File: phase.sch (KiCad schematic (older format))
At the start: 30 parts, among them U4 INA240A1PW, U5 UCC21520DW

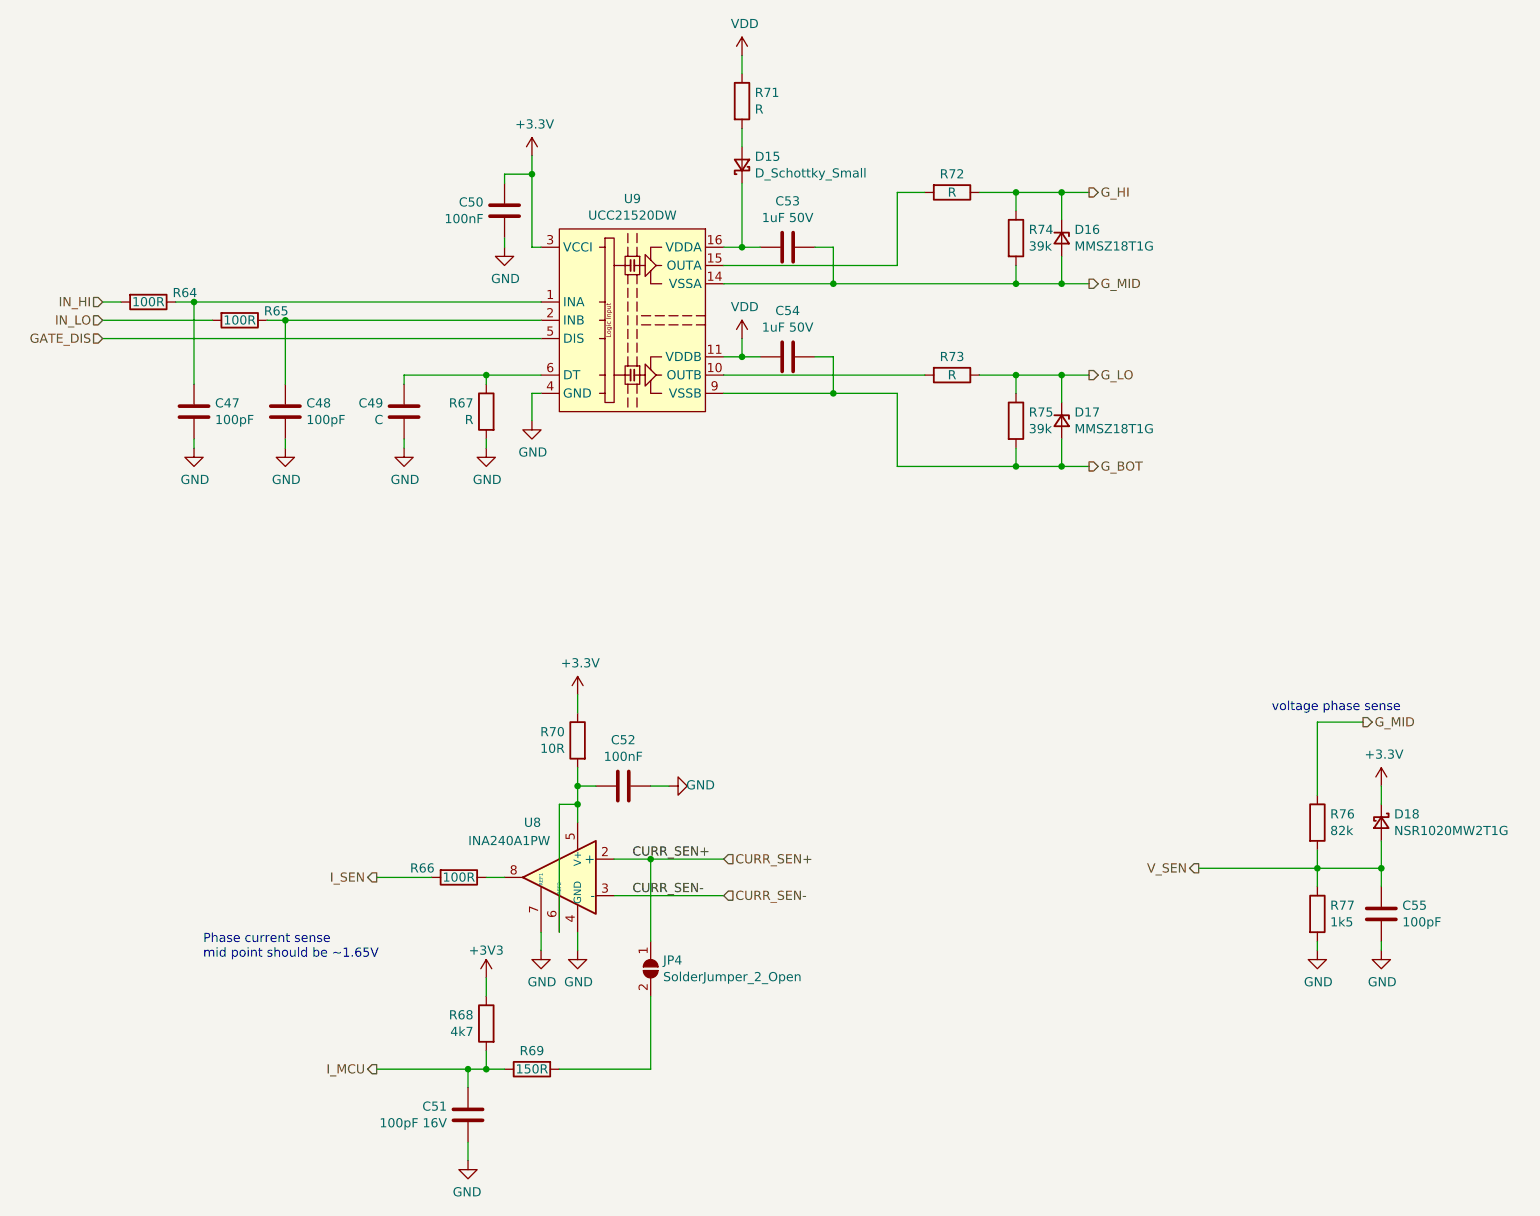
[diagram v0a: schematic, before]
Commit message: Routing nearly complete
some diodes made smaller
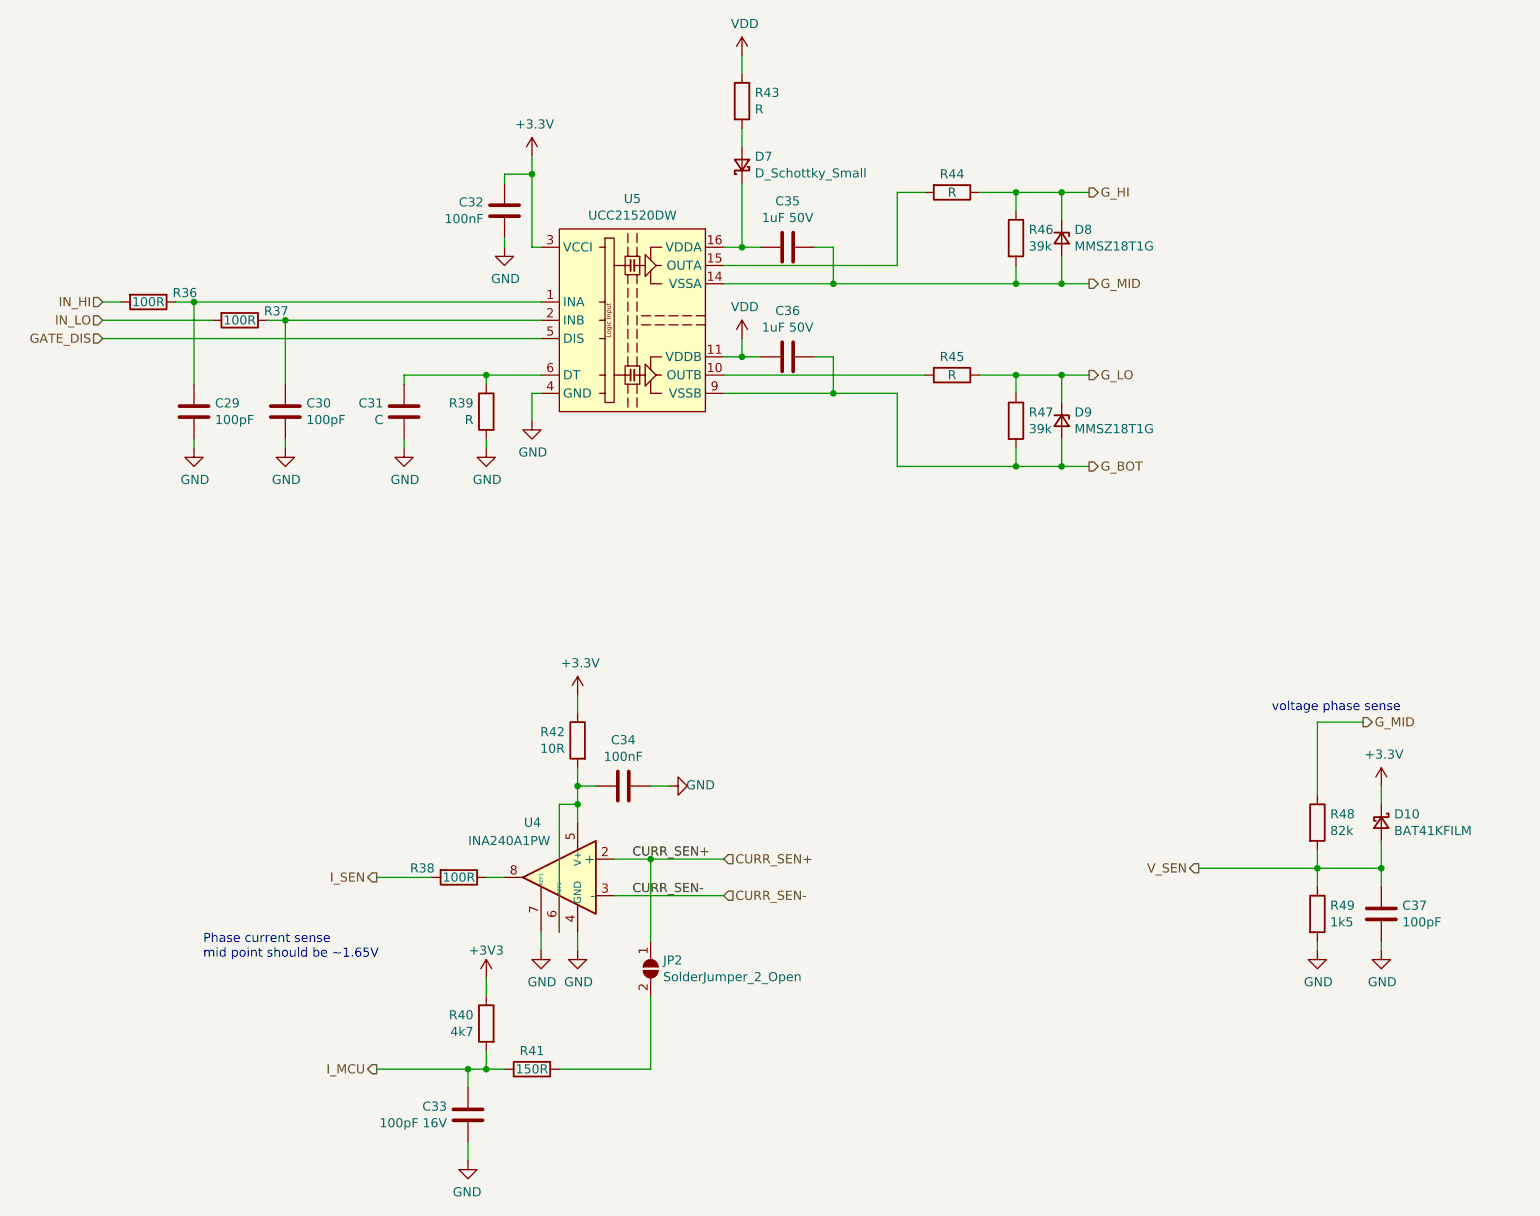
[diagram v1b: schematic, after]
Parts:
- D10: value NSR1020MW2T1G -> BAT41KFILM; footprint Diode_SMD:D_SOD-323 -> Diode_SMD:D_SOD-523
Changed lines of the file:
@@
 $Descr A4 11693 8268
 encoding utf-8
-Sheet 5 5
+Sheet 3 5
 Title "MESC_IMS_Ctrl"
 Date "2021-04-10"
@@
 AR Path="/6074FE4E/6070D5D5" Ref="U7"  Part="1"
 AR Path="/6075047A/6070D5D5" Ref="U9"  Part="1"
-F 0 "U9" H 5700 3115 50  0000 C CNN
+F 0 "U5" H 5700 3115 50  0000 C CNN
 F 1 "UCC21520DW" H 5700 3024 50  0000 C CNN
 F 2 "Package_SO:SOIC-16W_7.5x10.3mm_P1.27mm" H 5700 1900 50  0001 C CNN
@@
 AR Path="/6074FE4E/6071020A" Ref="U6"  Part="1"
 AR Path="/6075047A/6071020A" Ref="U8"  Part="1"
-F 0 "U8" H 5400 5800 50  0000 L CNN
+F 0 "U4" H 5400 5800 50  0000 L CNN
 F 1 "INA240A1PW" H 5350 5700 50  0000 L CNN
 F 2 "Package_SO:TSSOP-8_4.4x3mm_P0.65mm" H 5300 4850 50  0001 C CNN
@@
 AR Path="/6074FE4E/6071A2D5" Ref="C41"  Part="1"
 AR Path="/6075047A/6071A2D5" Ref="C50"  Part="1"
-F 0 "C50" H 4885 1896 50  0000 R CNN
+F 0 "C32" H 4885 1896 50  0000 R CNN
 F 1 "100nF" H 4885 1805 50  0000 R CNN
 F 2 "Capacitor_SMD:C_0402_1005Metric" H 5038 1700 50  0001 C CNN
@@
 AR Path="/6074FE4E/6071B90A" Ref="R56"  Part="1"
 AR Path="/6075047A/6071B90A" Ref="R70"  Part="1"
-F 0 "R70" H 5470 4796 50  0000 L CNN
+F 0 "R42" H 5470 4796 50  0000 L CNN
 F 1 "10R" H 5470 4705 50  0000 L CNN
 F 2 "Resistor_SMD:R_0402_1005Metric" V 5330 4750 50  0001 C CNN
@@
 AR Path="/6074FE4E/6071C3EC" Ref="R53"  Part="1"
 AR Path="/6075047A/6071C3EC" Ref="R67"  Part="1"
-F 0 "R67" H 4970 2996 50  0000 L CNN
+F 0 "R39" H 4970 2996 50  0000 L CNN
 F 1 "R" H 4970 2905 50  0000 L CNN
 F 2 "Resistor_SMD:R_0603_1608Metric" V 4830 2950 50  0001 C CNN
@@
 AR Path="/6074FE4E/6073CC35" Ref="R52"  Part="1"
 AR Path="/6075047A/6073CC35" Ref="R66"  Part="1"
-F 0 "R66" V 4700 5300 50  0000 C CNN
+F 0 "R38" V 4700 5300 50  0000 C CNN
 F 1 "100R" V 4750 5500 50  0000 C CNN
 F 2 "Resistor_SMD:R_0402_1005Metric" V 4680 5500 50  0001 C CNN
@@
 AR Path="/6074FE4E/6073DC29" Ref="C40"  Part="1"
 AR Path="/6075047A/6073DC29" Ref="C49"  Part="1"
-F 0 "C49" H 4336 2904 50  0000 R CNN
+F 0 "C31" H 4336 2904 50  0000 R CNN
 F 1 "C" H 4336 2995 50  0000 R CNN
 F 2 "Capacitor_SMD:C_0603_1608Metric" H 4488 2800 50  0001 C CNN
@@
 AR Path="/6074FE4E/60741D48" Ref="R62"  Part="1"
 AR Path="/6075047A/60741D48" Ref="R76"  Part="1"
-F 0 "R76" H 9520 5246 50  0000 L CNN
+F 0 "R48" H 9520 5246 50  0000 L CNN
 F 1 "82k" H 9520 5155 50  0000 L CNN
 F 2 "Resistor_SMD:R_0603_1608Metric" V 9380 5200 50  0001 C CNN
@@
 AR Path="/6074FE4E/6074271B" Ref="C46"  Part="1"
 AR Path="/6075047A/6074271B" Ref="C55"  Part="1"
-F 0 "C55" H 9915 5746 50  0000 L CNN
+F 0 "C37" H 9915 5746 50  0000 L CNN
 F 1 "100pF" H 9915 5655 50  0000 L CNN
 F 2 "Capacitor_SMD:C_0402_1005Metric" H 9838 5550 50  0001 C CNN
@@
 AR Path="/6074FE4E/607498EF" Ref="D14"  Part="1"
 AR Path="/6075047A/607498EF" Ref="D18"  Part="1"
-F 0 "D18" V 9754 5270 50  0000 L CNN
-F 1 "NSR1020MW2T1G" V 9845 5270 50  0000 L CNN
-F 2 "Diode_SMD:D_SOD-323" V 9800 5200 50  0001 C CNN
+F 0 "D10" V 9754 5270 50  0000 L CNN
+F 1 "BAT41KFILM" V 9845 5270 50  0000 L CNN
+F 2 "Diode_SMD:D_SOD-523" V 9800 5200 50  0001 C CNN
 F 3 "~" V 9800 5200 50  0001 C CNN
 	1    9800 5200
@@
 AR Path="/6074FE4E/60817438" Ref="D12"  Part="1"
 AR Path="/6075047A/60817438" Ref="D16"  Part="1"
-F 0 "D16" V 8004 2070 50  0000 L CNN
+F 0 "D8" V 8004 2070 50  0000 L CNN
 F 1 "MMSZ18T1G" V 8095 2070 50  0000 L CNN
 F 2 "Diode_SMD:D_SOD-123" V 8050 2000 50  0001 C CNN
@@
 AR Path="/6074FE4E/60818839" Ref="D13"  Part="1"
 AR Path="/6075047A/60818839" Ref="D17"  Part="1"
-F 0 "D17" V 8004 3070 50  0000 L CNN
+F 0 "D9" V 8004 3070 50  0000 L CNN
 F 1 "MMSZ18T1G" V 8095 3070 50  0000 L CNN
 F 2 "Diode_SMD:D_SOD-123" V 8050 3000 50  0001 C CNN
@@
 AR Path="/6074FE4E/60818EA3" Ref="R61"  Part="1"
 AR Path="/6075047A/60818EA3" Ref="R75"  Part="1"
-F 0 "R75" H 7870 3046 50  0000 L CNN
+F 0 "R47" H 7870 3046 50  0000 L CNN
 F 1 "39k" H 7870 2955 50  0000 L CNN
 F 2 "Resistor_SMD:R_0402_1005Metric" V 7730 3000 50  0001 C CNN
@@
 AR Path="/6074FE4E/608196FD" Ref="R60"  Part="1"
 AR Path="/6075047A/608196FD" Ref="R74"  Part="1"
-F 0 "R74" H 7870 2046 50  0000 L CNN
+F 0 "R46" H 7870 2046 50  0000 L CNN
 F 1 "39k" H 7870 1955 50  0000 L CNN
 F 2 "Resistor_SMD:R_0402_1005Metric" V 7730 2000 50  0001 C CNN
@@
 AR Path="/6074FE4E/6142D824" Ref="C44"  Part="1"
 AR Path="/6075047A/6142D824" Ref="C53"  Part="1"
-F 0 "C53" V 6298 2050 50  0000 C CNN
+F 0 "C35" V 6298 2050 50  0000 C CNN
 F 1 "1uF 50V" V 6389 2050 50  0000 C CNN
 F 2 "Capacitor_SMD:C_0603_1608Metric" H 6588 1900 50  0001 C CNN
@@
 AR Path="/6074FE4E/61533BA1" Ref="C45"  Part="1"
 AR Path="/6075047A/61533BA1" Ref="C54"  Part="1"
-F 0 "C54" V 6298 2650 50  0000 C CNN
+F 0 "C36" V 6298 2650 50  0000 C CNN
 F 1 "1uF 50V" V 6389 2650 50  0000 C CNN
 F 2 "Capacitor_SMD:C_0603_1608Metric" H 6588 2500 50  0001 C CNN
@@
 AR Path="/6074FE4E/61559AE4" Ref="D11"  Part="1"
 AR Path="/6075047A/61559AE4" Ref="D15"  Part="1"
-F 0 "D15" V 6346 1530 50  0000 R CNN
+F 0 "D7" V 6346 1530 50  0000 R CNN
 F 1 "D_Schottky_Small" V 6255 1530 50  0000 R CNN
 F 2 "Diode_SMD:D_SOD-128" V 6300 1600 50  0001 C CNN
@@
 AR Path="/6074FE4E/6155C6AD" Ref="R57"  Part="1"
 AR Path="/6075047A/6155C6AD" Ref="R71"  Part="1"
-F 0 "R71" H 6370 1296 50  0000 L CNN
+F 0 "R43" H 6370 1296 50  0000 L CNN
 F 1 "R" H 6370 1205 50  0000 L CNN
 F 2 "Resistor_SMD:R_0805_2012Metric" V 6230 1250 50  0001 C CNN
@@
 AR Path="/6074FE4E/6157E0B0" Ref="R59"  Part="1"
 AR Path="/6075047A/6157E0B0" Ref="R73"  Part="1"
-F 0 "R73" V 7350 2750 50  0000 C CNN
+F 0 "R45" V 7350 2750 50  0000 C CNN
 F 1 "R" V 7450 2750 50  0000 C CNN
 F 2 "Resistor_SMD:R_0805_2012Metric" V 7380 2750 50  0001 C CNN
@@
 AR Path="/6074FE4E/6157E522" Ref="R58"  Part="1"
 AR Path="/6075047A/6157E522" Ref="R72"  Part="1"
-F 0 "R72" V 7350 1750 50  0000 C CNN
+F 0 "R44" V 7350 1750 50  0000 C CNN
 F 1 "R" V 7450 1750 50  0000 C CNN
 F 2 "Resistor_SMD:R_0805_2012Metric" V 7380 1750 50  0001 C CNN
@@
 AR Path="/6074FE4E/61584985" Ref="C38"  Part="1"
 AR Path="/6075047A/61584985" Ref="C47"  Part="1"
-F 0 "C47" H 3415 2996 50  0000 L CNN
+F 0 "C29" H 3415 2996 50  0000 L CNN
 F 1 "100pF" H 3415 2905 50  0000 L CNN
 F 2 "Capacitor_SMD:C_0402_1005Metric" H 3338 2800 50  0001 C CNN
@@
 AR Path="/6074FE4E/61587154" Ref="C39"  Part="1"
 AR Path="/6075047A/61587154" Ref="C48"  Part="1"
-F 0 "C48" H 3915 2996 50  0000 L CNN
+F 0 "C30" H 3915 2996 50  0000 L CNN
 F 1 "100pF" H 3915 2905 50  0000 L CNN
 F 2 "Capacitor_SMD:C_0402_1005Metric" H 3838 2800 50  0001 C CNN
@@
 AR Path="/6074FE4E/6158B03C" Ref="R50"  Part="1"
 AR Path="/6075047A/6158B03C" Ref="R64"  Part="1"
-F 0 "R64" V 3000 2550 50  0000 C CNN
+F 0 "R36" V 3000 2550 50  0000 C CNN
 F 1 "100R" V 3050 2350 50  0000 C CNN
 F 2 "Resistor_SMD:R_0402_1005Metric" V 2980 2350 50  0001 C CNN
@@
 AR Path="/6074FE4E/6158BFEB" Ref="R51"  Part="1"
 AR Path="/6075047A/6158BFEB" Ref="R65"  Part="1"
-F 0 "R65" V 3500 2650 50  0000 C CNN
+F 0 "R37" V 3500 2650 50  0000 C CNN
 F 1 "100R" V 3550 2450 50  0000 C CNN
 F 2 "Resistor_SMD:R_0402_1005Metric" V 3480 2450 50  0001 C CNN
@@
 AR Path="/6074FE4E/61DEE963" Ref="C43"  Part="1"
 AR Path="/6075047A/61DEE963" Ref="C52"  Part="1"
-F 0 "C52" V 5398 5000 50  0000 C CNN
+F 0 "C34" V 5398 5000 50  0000 C CNN
 F 1 "100nF" V 5489 5000 50  0000 C CNN
 F 2 "Capacitor_SMD:C_0402_1005Metric" H 5688 4850 50  0001 C CNN
@@
 AR Path="/6074FE4E/6091D253" Ref="C42"  Part="1"
 AR Path="/6075047A/6091D253" Ref="C51"  Part="1"
-F 0 "C51" H 4915 6846 50  0000 L CNN
+F 0 "C33" H 4915 6846 50  0000 L CNN
 F 1 "100pF 16V" H 4915 6755 50  0000 L CNN
 F 2 "Capacitor_SMD:C_0402_1005Metric" H 4838 6650 50  0001 C CNN
@@
 AR Path="/6074FE4E/6091D25A" Ref="R55"  Part="1"
 AR Path="/6075047A/6091D25A" Ref="R69"  Part="1"
-F 0 "R69" V 5050 6550 50  0000 C CNN
+F 0 "R41" V 5050 6550 50  0000 C CNN
 F 1 "150R" V 5150 6550 50  0000 C CNN
 F 2 "Resistor_SMD:R_0402_1005Metric" V 5080 6550 50  0001 C CNN
@@
 AR Path="/6074FE4E/6091D261" Ref="R54"  Part="1"
 AR Path="/6075047A/6091D261" Ref="R68"  Part="1"
-F 0 "R68" H 4970 6346 50  0000 L CNN
+F 0 "R40" H 4970 6346 50  0000 L CNN
 F 1 "4k7" H 4970 6255 50  0000 L CNN
 F 2 "Resistor_SMD:R_0402_1005Metric" V 4830 6300 50  0001 C CNN
@@
 AR Path="/6074FE4E/60742356" Ref="R63"  Part="1"
 AR Path="/6075047A/60742356" Ref="R77"  Part="1"
-F 0 "R77" H 9520 5746 50  0000 L CNN
+F 0 "R49" H 9520 5746 50  0000 L CNN
 F 1 "1k5" H 9520 5655 50  0000 L CNN
 F 2 "Resistor_SMD:R_0603_1608Metric" V 9380 5700 50  0001 C CNN
@@
 AR Path="/6074FE4E/60924C9F" Ref="JP3"  Part="1"
 AR Path="/6075047A/60924C9F" Ref="JP4"  Part="1"
-F 0 "JP4" V 5754 6068 50  0000 L CNN
+F 0 "JP2" V 5754 6068 50  0000 L CNN
 F 1 "SolderJumper_2_Open" V 5845 6068 50  0000 L CNN
 F 2 "Jumper:SolderJumper-2_P1.3mm_Open_RoundedPad1.0x1.5mm" H 5800 6000 50  0001 C CNN

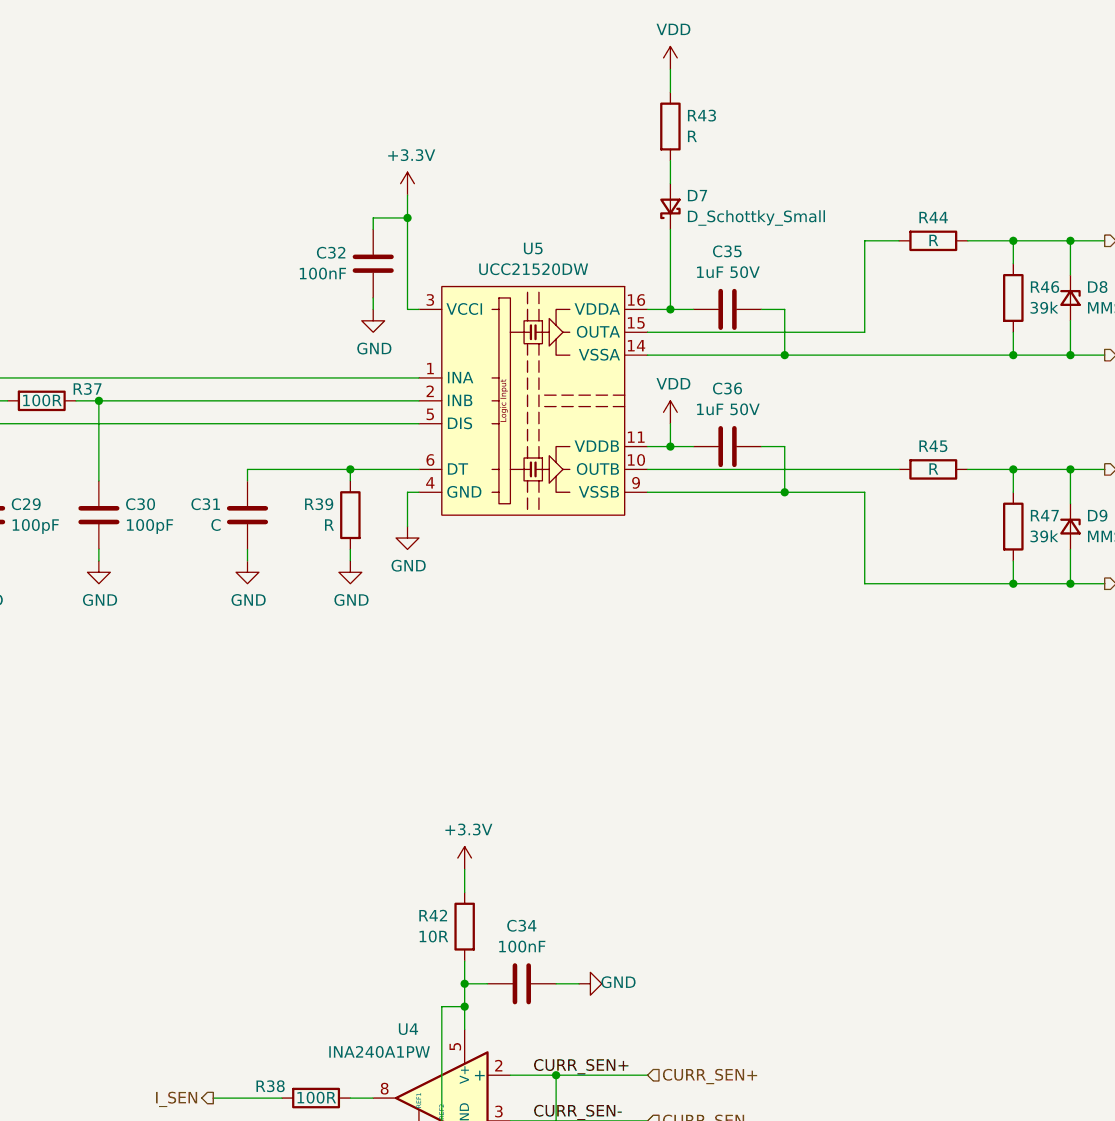
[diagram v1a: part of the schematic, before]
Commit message: Updated part numbers
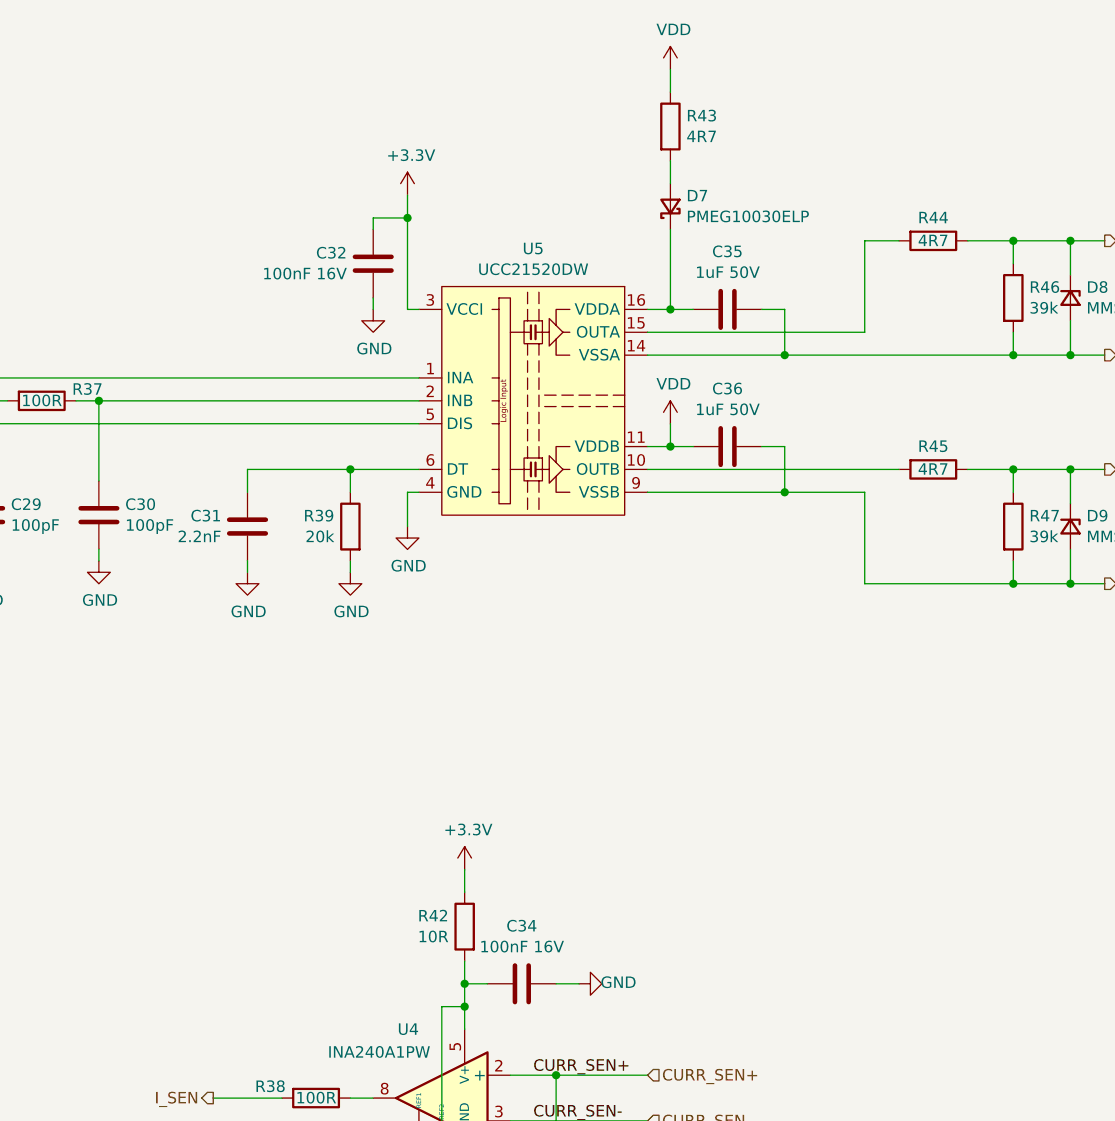
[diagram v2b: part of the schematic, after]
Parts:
- C29, C30, C33, C35, C36, C37, D8, D9, JP2, R36, R37, R38, R40, R41, R42, R46, R47, U4: Checked (none) -> Yes
- C31: value C -> 2.2nF; Checked (none) -> Yes; LCSC (none) -> C1604
- C32, C34: value 100nF -> 100nF 16V; Checked (none) -> Yes
- D10: Checked (none) -> Yes; LCSC (none) -> C73150
- D7: value D_Schottky_Small -> PMEG10030ELP; Checked (none) -> Yes; LCSC (none) -> C503376
- R39: value R -> 20k; Checked (none) -> Yes; LCSC (none) -> C4184
- R43, R44, R45: value R -> 4R7; Checked (none) -> Yes; LCSC (none) -> C17675
- R48: Checked (none) -> Yes; LCSC C4142 -> C23254
- R49: Checked (none) -> Yes; LCSC C25867 -> C22843
- U5: Checked (none) -> Yes; LCSC C601651 -> C189707
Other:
- moved on the sheet: C31, R39
